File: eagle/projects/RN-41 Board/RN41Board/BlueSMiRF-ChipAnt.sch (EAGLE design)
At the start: 18 parts, among them Q1 MOSFET-NCHANNELSMD, U1 BLUETOOTH-RN41, U3 3.3V

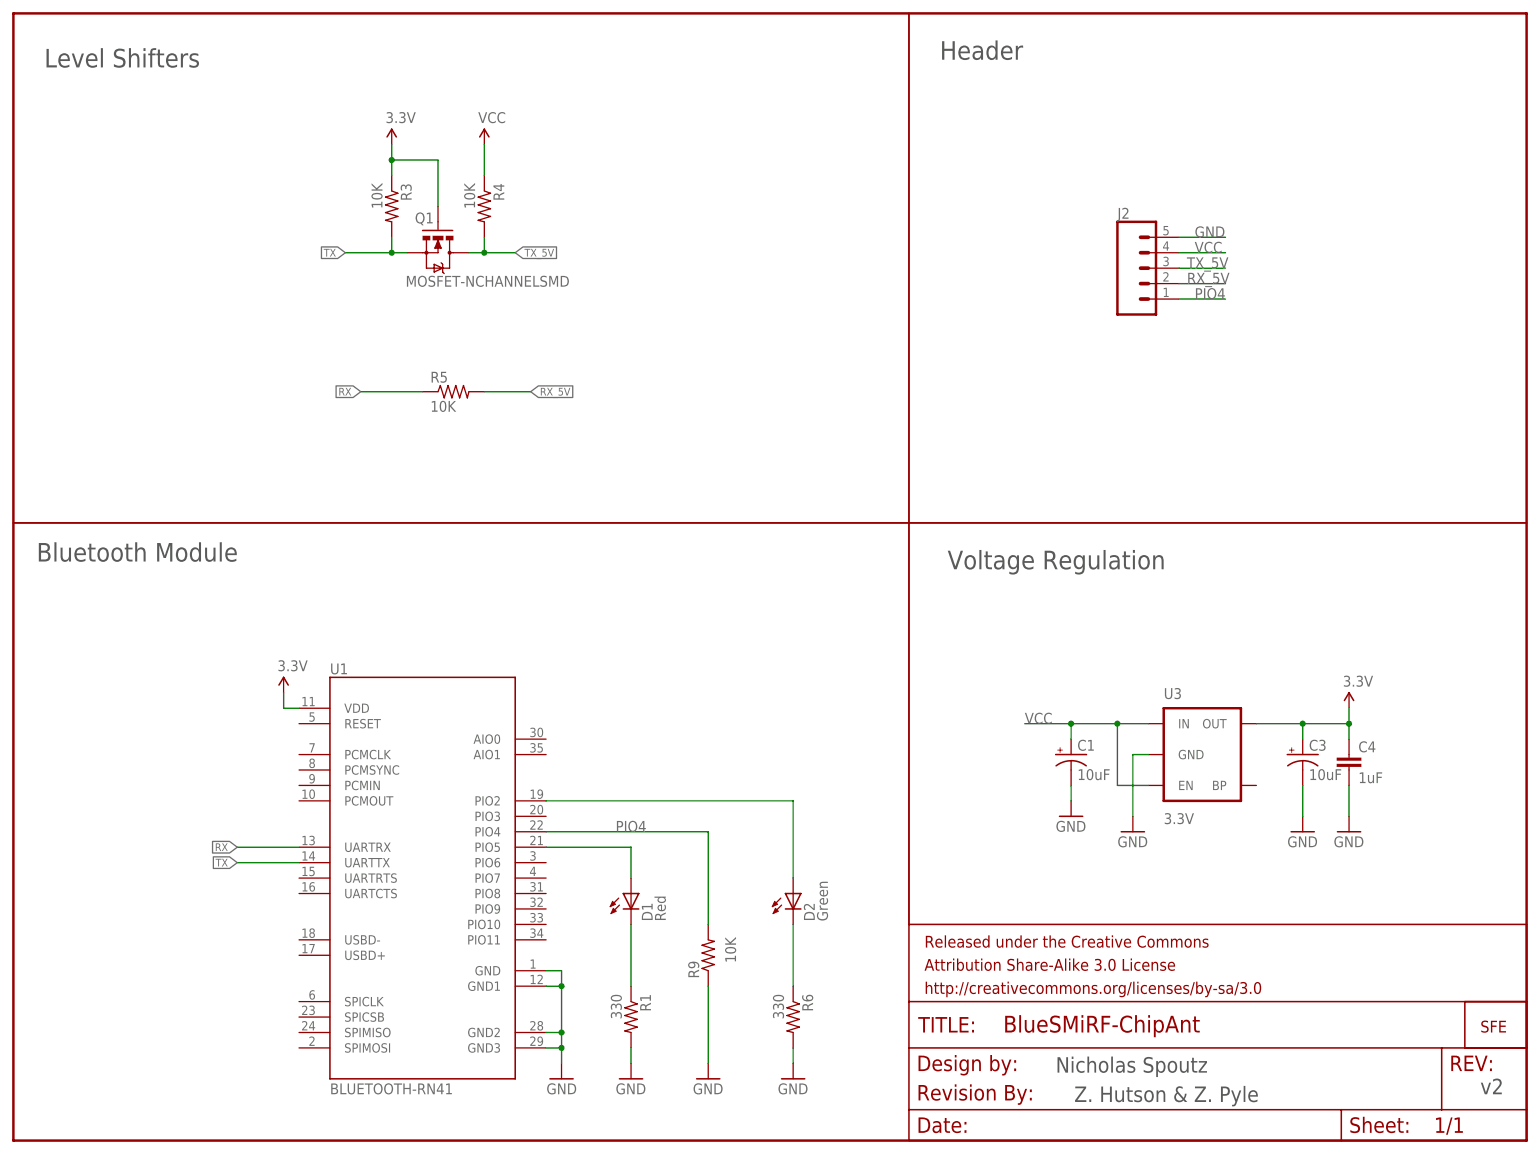
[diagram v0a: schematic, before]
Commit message: Changed PIO4 to PIO2
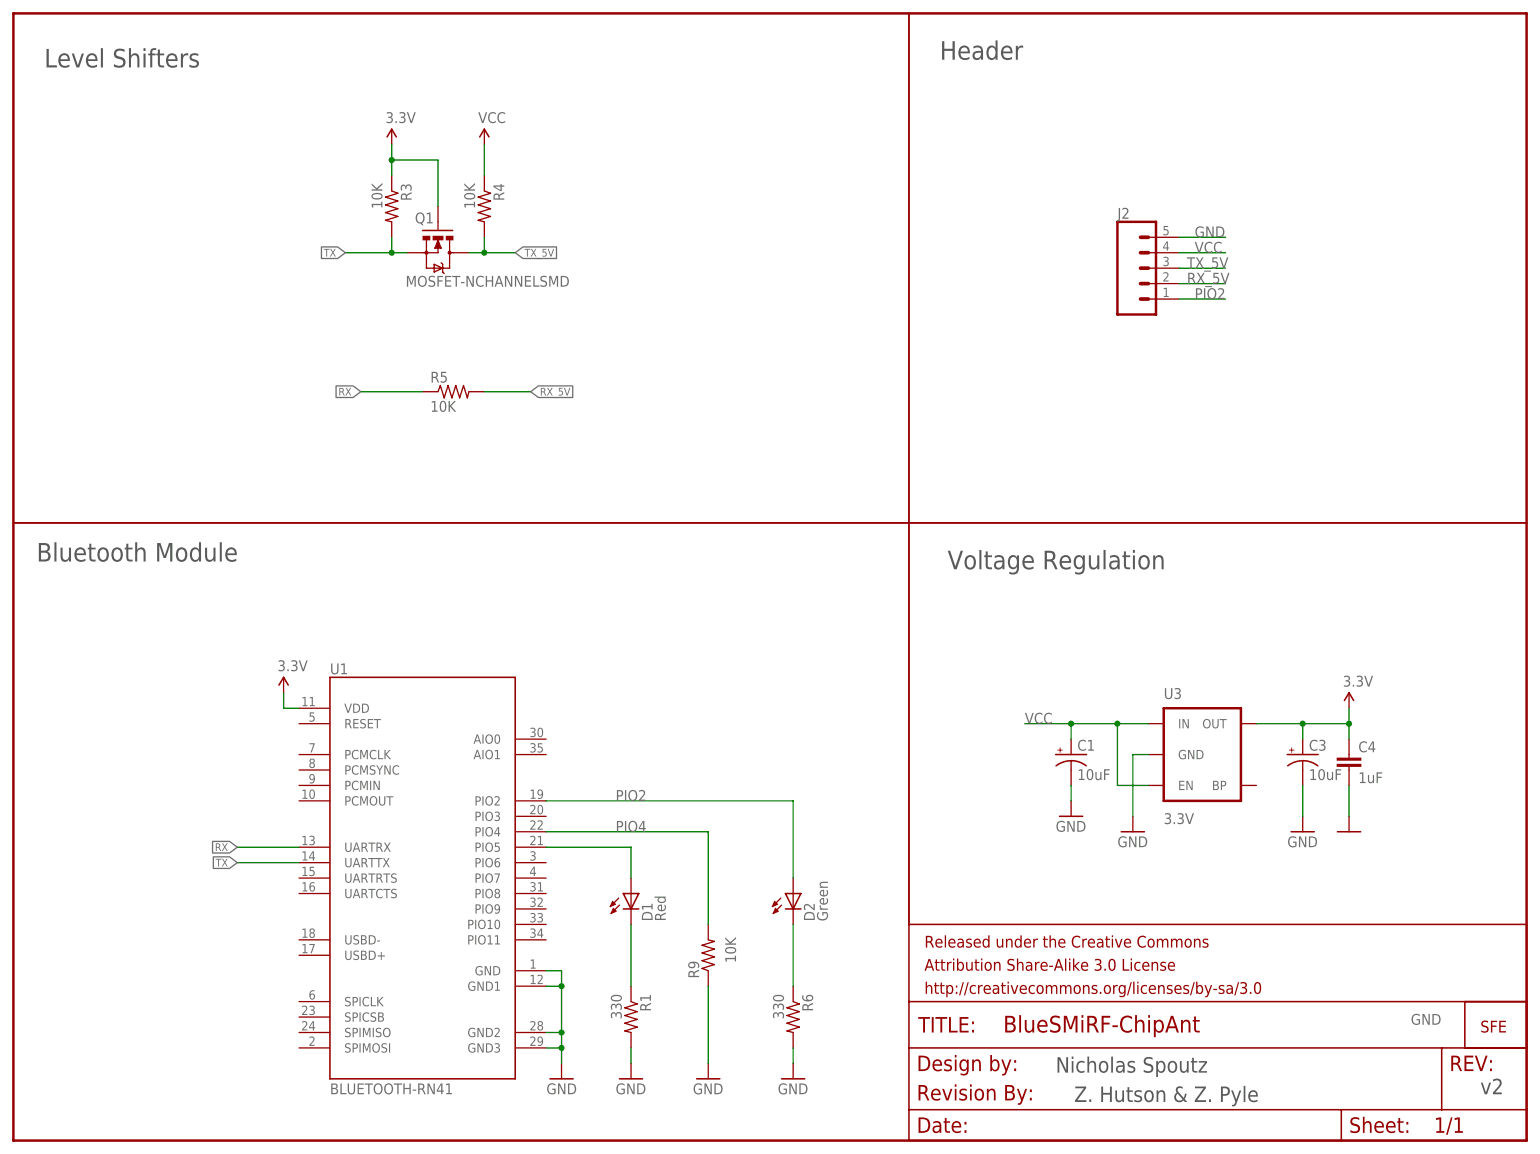
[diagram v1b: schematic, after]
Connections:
- removed net N$2: D2.A, U1.PIO2
- new net PIO2: D2.A, J2.1, U1.PIO2
- net PIO4: no longer J2.1
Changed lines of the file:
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@@
 </instance>
 <instance part="GND3" gate="1" x="219.71" y="50.8" smashed="yes">
-<attribute name="VALUE" x="217.17" y="48.26" size="1.778" layer="96"/>
+<attribute name="VALUE" x="229.87" y="19.05" size="1.778" layer="96"/>
 </instance>
 <instance part="P+2" gate="1" x="219.71" y="71.12" smashed="yes">
@@
 </segment>
 </net>
-<net name="N$2" class="0">
+<net name="PIO2" class="0">
 <segment>
 <wire x1="87.63" y1="55.88" x2="128.27" y2="55.88" width="0.1524" layer="91"/>
@@
 <pinref part="U1" gate="G$1" pin="PIO2"/>
 <pinref part="D2" gate="G$1" pin="A"/>
+<label x="99.06" y="55.88" size="1.778" layer="95"/>
+</segment>
+<segment>
+<pinref part="J2" gate="G$1" pin="1"/>
+<wire x1="191.77" y1="138.43" x2="199.39" y2="138.43" width="0.1524" layer="91"/>
+<label x="194.31" y="138.43" size="1.778" layer="95"/>
 </segment>
 </net>
@@
 <pinref part="R9" gate="G$1" pin="2"/>
 </segment>
-<segment>
-<pinref part="J2" gate="G$1" pin="1"/>
-<wire x1="191.77" y1="138.43" x2="199.39" y2="138.43" width="0.1524" layer="91"/>
-<label x="194.31" y="138.43" size="1.778" layer="95"/>
-</segment>
-</net>
+</net>
